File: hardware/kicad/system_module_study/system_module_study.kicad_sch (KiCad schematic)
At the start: 16 parts, among them J1 FC_TBD, J10 MOTOR_2_TBD, J11 MOTOR_3_TBD, J12 MOTOR_4_TBD, J13 MOTOR_5_TBD, J14 MOTOR_6_TBD, J15 POWER_DISTRIBUTION_BEC_TBD, J2 RX_TBD, J3 ESC_CH1_TBD, J4 ESC_CH2_TBD, J5 ESC_CH3_TBD, J6 ESC_CH4_TBD, J7 ESC_CH5_TBD, J8 ESC_CH6_TBD, J9 MOTOR_1_TBD

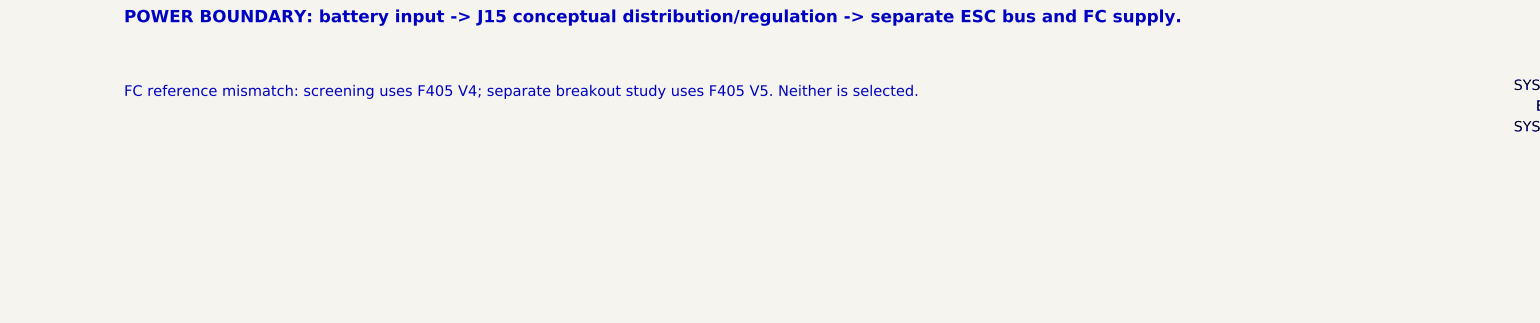
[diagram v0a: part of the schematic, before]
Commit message: docs: map Gazebo rotor indices to Hexa X study
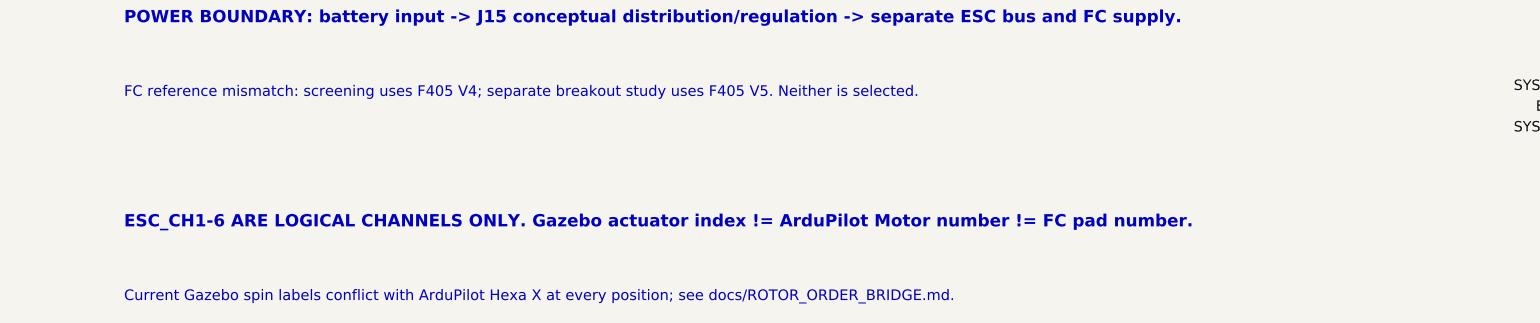
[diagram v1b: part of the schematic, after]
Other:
- note added: "Current Gazebo spin labels conflict with ArduPilot Hexa X at every position; see docs/ROTOR_ORDER_BRIDGE.md."
- note added: "ESC_CH1-6 ARE LOGICAL CHANNELS ONLY. Gazebo actuator index != ArduPilot Motor number != FC pad number."
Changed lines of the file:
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@@
+		)
+	)
+	(text "ESC_CH1-6 ARE LOGICAL CHANNELS ONLY. Gazebo actuator index != ArduPilot Motor number != FC pad number."
+		(exclude_from_sim no)
+		(at 25 230 0)
+		(effects
+			(font
+				(size 1.5 1.5)
+				(bold yes)
+			)
+			(justify left bottom)
+		)
+	)
+	(text "Current Gazebo spin labels conflict with ArduPilot Hexa X at every position; see docs/ROTOR_ORDER_BRIDGE.md."
+		(exclude_from_sim no)
+		(at 25 239 0)
+		(effects
+			(font
+				(size 1.3 1.3)
+			)
+			(justify left bottom)
 		)
 	)

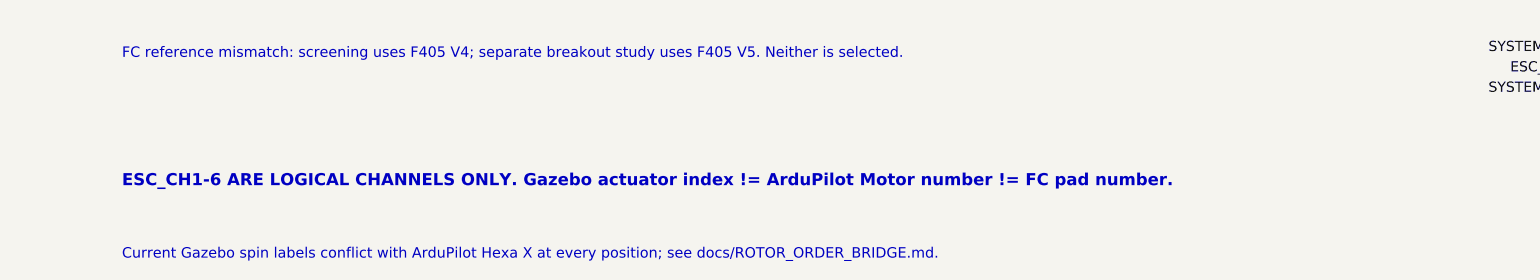
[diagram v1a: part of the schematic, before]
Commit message: feat: check Hexa X rotor order with explicit nose orientation
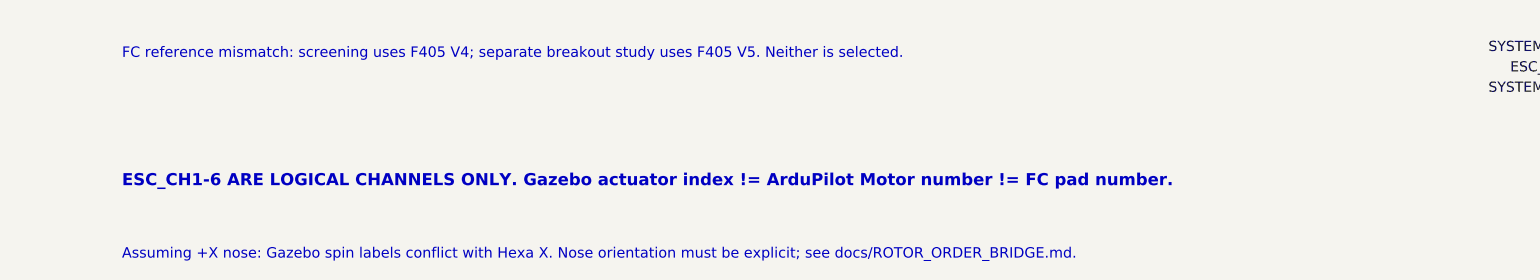
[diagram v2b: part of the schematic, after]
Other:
- note added: "Assuming +X nose: Gazebo spin labels conflict with Hexa X. Nose orientation must be explicit; see docs/ROTOR_ORDER_BRIDGE.md."
- note removed: "Current Gazebo spin labels conflict with ArduPilot Hexa X at every position; see docs/ROTOR_ORDER_BRIDGE.md."
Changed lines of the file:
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@@
 		)
 	)
-	(text "Current Gazebo spin labels conflict with ArduPilot Hexa X at every position; see docs/ROTOR_ORDER_BRIDGE.md."
+	(text "Assuming +X nose: Gazebo spin labels conflict with Hexa X. Nose orientation must be explicit; see docs/ROTOR_ORDER_BRIDGE.md."
 		(exclude_from_sim no)
 		(at 25 239 0)
